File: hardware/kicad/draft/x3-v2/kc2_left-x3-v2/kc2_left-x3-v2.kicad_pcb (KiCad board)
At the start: 2 copper layers, 136.3 x 127.8 mm, 67 parts, among them SW1 KEY_01, SW10 KEY_10, SW11 KEY_11, SW12 KEY_12, SW13 KEY_13, SW14 KEY_14, SW15 KEY_15, SW16 KEY_16, SW17 KEY_17, SW18 KEY_18, SW19 KEY_19, SW2 KEY_02, SW20 KEY_20, SW21 KEY_21, SW22 KEY_22, SW23 KEY_23, SW24 KEY_24, SW25 KEY_25, SW26 KEY_26, SW27 KEY_27, SW28 KEY_28, SW29 KEY_29, SW3 KEY_03, SW30 KEY_30, SW31 KEY_31, SW32 KEY_32, SW4 KEY_04, SW5 KEY_05, SW6 KEY_06, SW7 KEY_07, SW8 KEY_08, SW9 KEY_09, U1 nice!nano_v2_socket_24pin

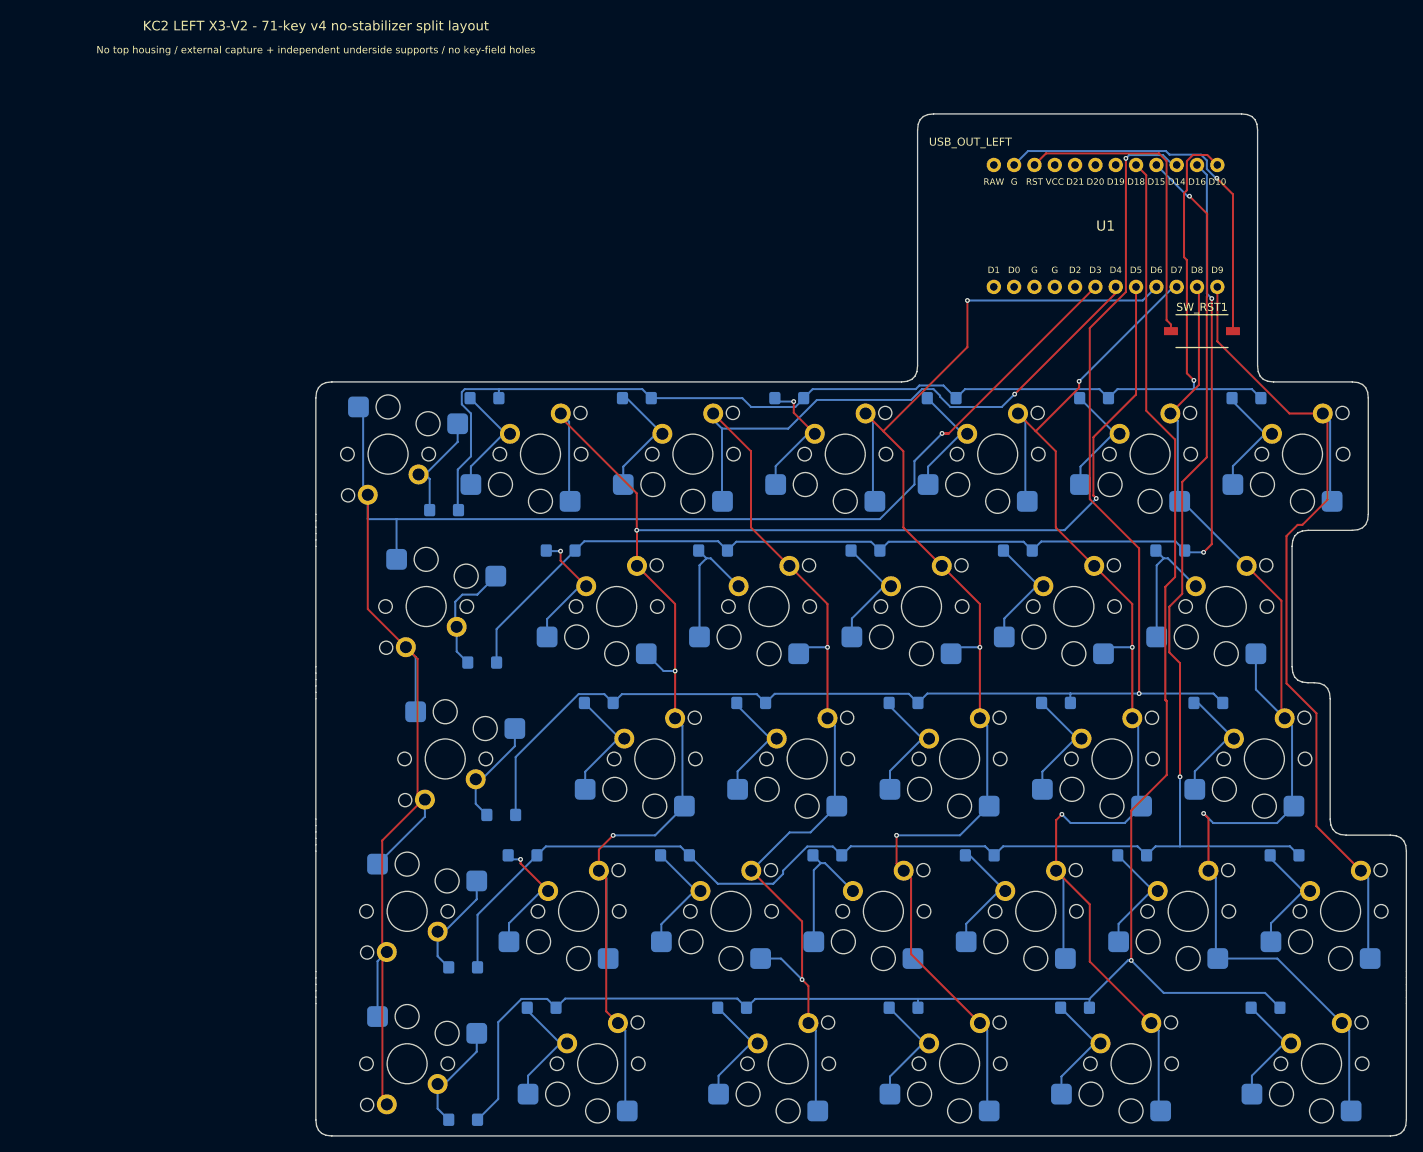
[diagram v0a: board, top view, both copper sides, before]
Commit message: feat(hardware): complete KC2 X3 V2 digital draft
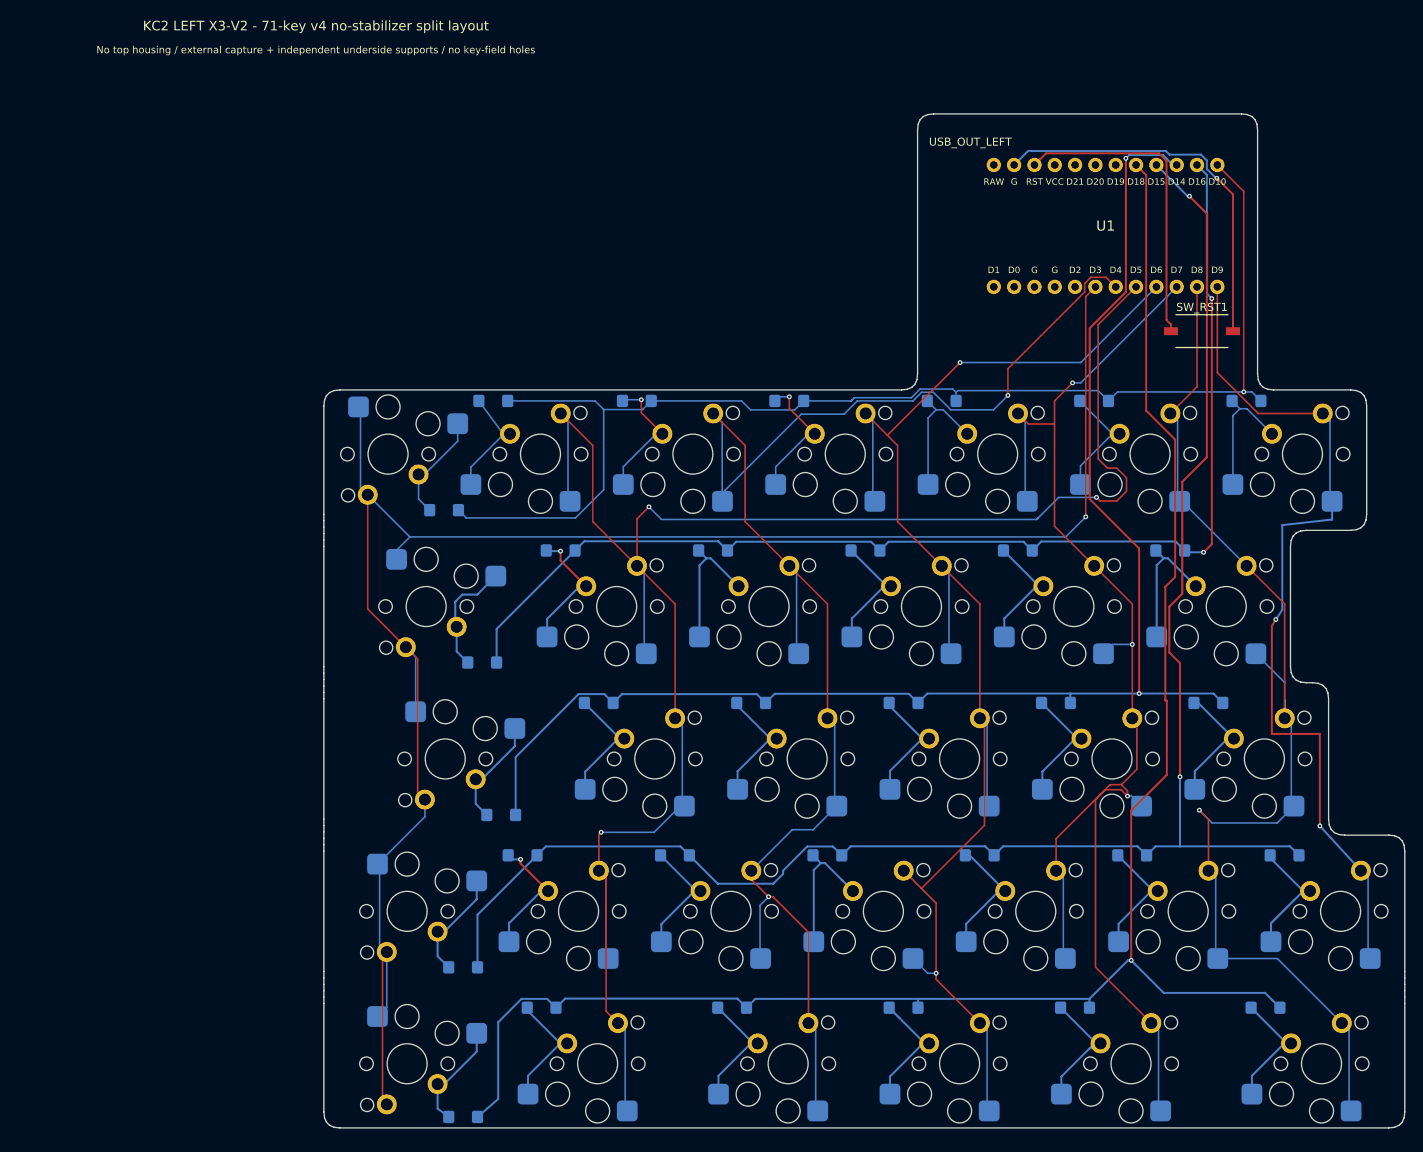
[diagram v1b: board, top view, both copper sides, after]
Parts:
- moved D2 1.15 mm to (57.2, 70.9)
- moved D27 0.35 mm to (53.4, 160.4)
- moved D3 0.35 mm to (75.1, 70.9)
- moved D4 0.35 mm to (94.2, 70.9)
- moved D5 0.35 mm to (113.2, 70.9)
- moved D6 0.35 mm to (132.3, 70.9)
- moved D7 0.35 mm to (151.3, 70.9)
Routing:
- net L_COL1: track 217.9 -> 238.0 mm, vias 4 -> 3
- net L_COL2: track 183.6 -> 199.6 mm, vias 3 -> 2
- net L_COL4: track 162.0 -> 172.4 mm
- net LK26_D: track 15.0 -> 21.6 mm
- net L_ROW0: track 155.5 -> 159.4 mm
- net L_COL5: track 144.5 -> 147.8 mm
- net L_COL3: track 179.7 -> 182.6 mm, vias 3 -> 2
- net LK31_D: track 15.0 -> 17.2 mm
- net L_ROW4: track 224.8 -> 227.0 mm
- net LK19_D: track 15.7 -> 17.8 mm
- net LK23_D: track 17.0 -> 19.0 mm
- net LK30_D: track 15.0 -> 16.9 mm
- net L_ROW3: track 210.6 -> 212.2 mm
- net LK07_D: track 15.0 -> 16.5 mm
- net LK05_D: track 15.0 -> 16.4 mm
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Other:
- board size 136.3 x 127.8 mm -> 135.1 x 126.8 mm

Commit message: fix: add X3 V2 diode edge clearance
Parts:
- moved D27 4.42 mm to (55.9, 156.7)
- moved D3 4.29 mm to (72.9, 74.5)
- moved D4 4.29 mm to (91.9, 74.5)
- moved D5 4.29 mm to (111.0, 74.5)
- moved D6 4.29 mm to (130.0, 74.5)
- moved D7 4.29 mm to (149.1, 74.5)
- moved D2 1.38 mm to (58.1, 71.9)
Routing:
- net L_COL1: track 238.0 -> 203.6 mm, vias 3 -> 4
- net L_COL3: track 182.6 -> 152.7 mm, vias 2 -> 4
- net L_ROW1: track 150.1 -> 168.5 mm, vias 2 -> 1
- net L_COL0: track 236.8 -> 222.4 mm, vias 1 -> 0
- net L_COL2: track 199.6 -> 187.5 mm
- net RST: track 40.0 -> 28.5 mm
- net L_COL4: track 172.4 -> 161.2 mm, vias 3 -> 2
- net L_ROW2: track 182.3 -> 172.8 mm, vias 2 -> 1
- net L_COL6: track 109.0 -> 117.1 mm, vias 2 -> 0
- net LK26_D: track 21.6 -> 15.6 mm
- net LK23_D: track 19.0 -> 15.0 mm
- net LK04_D: track 16.8 -> 13.7 mm, vias 1 -> 0
- net LK07_D: track 16.5 -> 13.5 mm
- net LK03_D: track 16.6 -> 13.6 mm, vias 1 -> 0
- net LK05_D: track 16.4 -> 13.5 mm
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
